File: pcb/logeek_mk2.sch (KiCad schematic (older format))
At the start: 136 parts, among them P1 Power, P10 XH2.54-2P RA, P11 BARREL_JACK, P12 USB_B, P13 DC3 5x2, P14 Power, P15 Analog, P16 Digital, P17 Digital, P2 Analog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

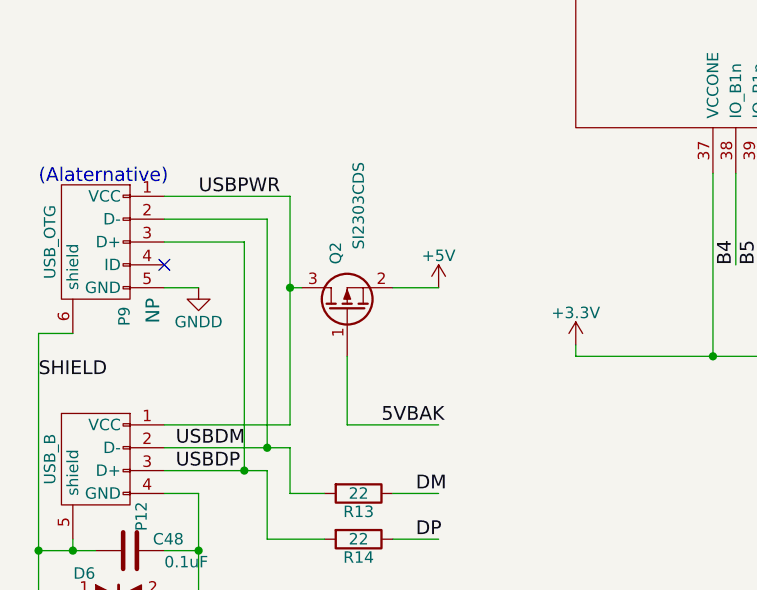
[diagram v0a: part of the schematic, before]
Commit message: Fine-tune copper and silkscreen. Add a fuse on USB power input.
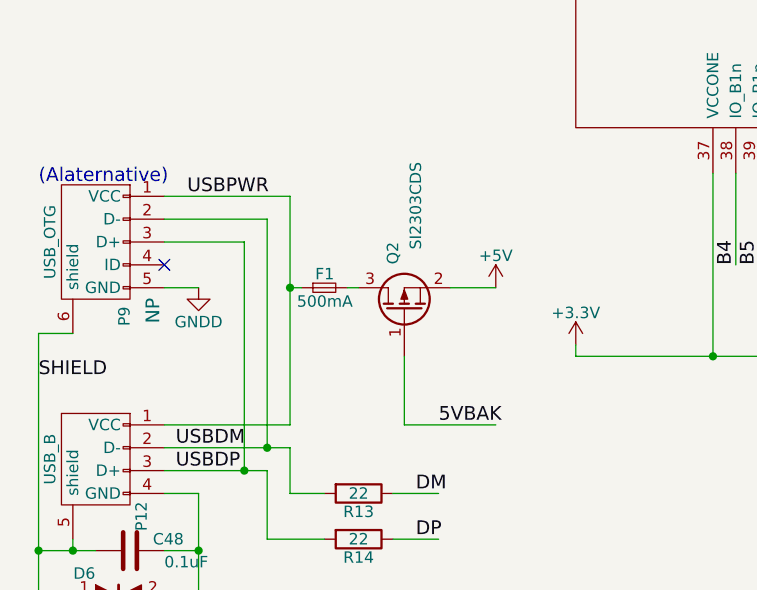
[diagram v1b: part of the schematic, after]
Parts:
- added F1: 500mA, Resistors_SMD:R_0603_HandSoldering, symbol F_Small
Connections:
- wire segments 545 -> 546
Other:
- moved on the sheet: Q2

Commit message: Power input socket changed to 5.08mm terminal.
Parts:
- P10: footprint Logeek_MK2:PINHEAD1-2 -> Logeek_MK2:DG301_2P_5.08mm_Straight
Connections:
- net labels removed: A8
- wire segments 546 -> 545
- no-connect marks 24 -> 25

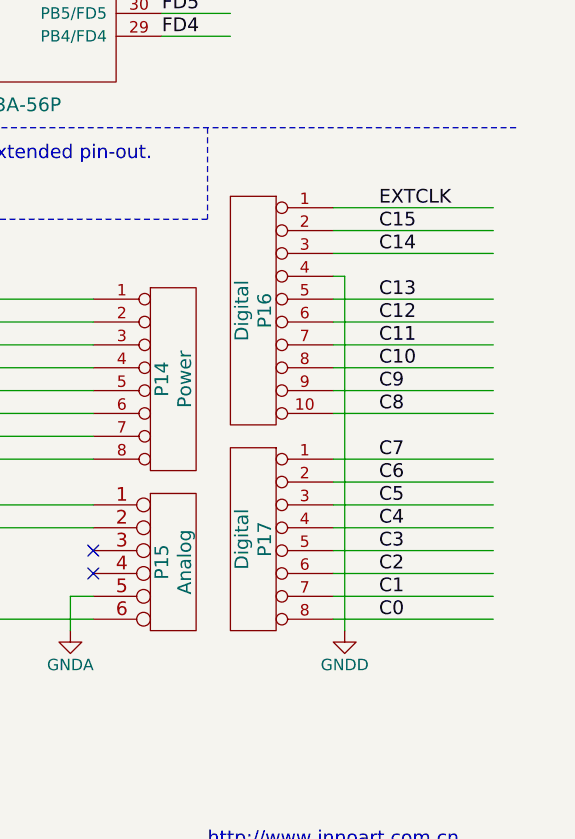
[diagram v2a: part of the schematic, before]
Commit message: C14,C15,CLK and GND pins changed.
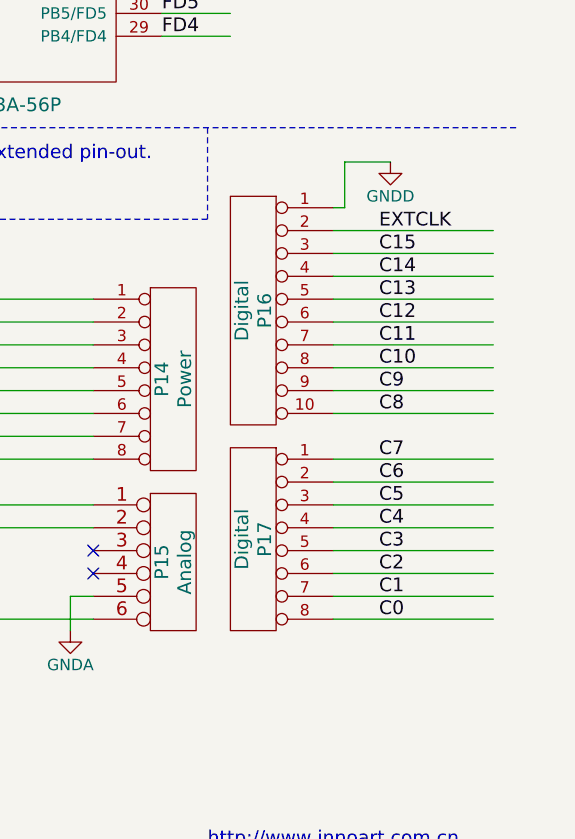
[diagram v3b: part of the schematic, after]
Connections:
- wire segments 545 -> 546
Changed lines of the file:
@@
 Text Label 15450 8150 0    60   ~ 0
 C13
-Text Label 15450 7950 0    60   ~ 0
+Text Label 15450 8050 0    60   ~ 0
 C14
-Text Label 15450 7850 0    60   ~ 0
+Text Label 15450 7950 0    60   ~ 0
 C15
 $Comp
 L GNDD #PWR0104
 U 1 1 55B9ECF4
-P 15300 9600
-F 0 "#PWR0104" H 15300 9350 50  0001 C CNN
-F 1 "GNDD" H 15300 9450 50  0000 C CNN
-F 2 "" H 15300 9600 60  0000 C CNN
-F 3 "" H 15300 9600 60  0000 C CNN
-	1    15300 9600
+P 15500 7550
+F 0 "#PWR0104" H 15500 7300 50  0001 C CNN
+F 1 "GNDD" H 15500 7400 50  0000 C CNN
+F 2 "" H 15500 7550 60  0000 C CNN
+F 3 "" H 15500 7550 60  0000 C CNN
+	1    15500 7550
 	1    0    0    -1
 $EndComp
-Text Label 15450 7750 0    60   ~ 0
+Text Label 15450 7850 0    60   ~ 0
 EXTCLK
 $Comp
@@
 Connection ~ 1100 8900
 Wire Wire Line
-	15300 8050 15300 9600
-Wire Wire Line
-	15950 7750 15250 7750
-Wire Wire Line
 	15950 7850 15250 7850
 Wire Wire Line
@@
 	13450 9550 14200 9550
 Wire Wire Line
-	15300 8050 15250 8050
-Wire Wire Line
 	14100 9450 14200 9450
 Wire Notes Line
@@
 	2350 7750 2300 7750
 NoConn ~ 14200 9250
+Wire Wire Line
+	15950 8050 15250 8050
+Wire Wire Line
+	15250 7750 15300 7750
+Wire Wire Line
+	15300 7750 15300 7550
+Wire Wire Line
+	15300 7550 15500 7550
 $EndSCHEMATC

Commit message: Power supplies redesigned.
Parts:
- removed D2, D7: 1N5819WS, Diodes_SMD:SOD-123, symbol D_Schottky
- removed D4, D8: 1N4148WS, Diodes_SMD:SOD-323, symbol D_Schottky
- removed F1: 500mA, Resistors_SMD:R_0603_HandSoldering, symbol F_Small
- removed R13, R14: 22, Resistors_SMD:R_0402_HandSoldering, symbol R
- removed R31: 1000k, Resistors_SMD:R_0402_HandSoldering, symbol R
- removed R39: 10k, Resistors_SMD:R_0402_HandSoldering, symbol R
- added L3: DLW21SN900SQ2, Logeek_MK2:CommonModeChoke_0805, symbol CMCC
- added Q1: SI2302CDS, Housings_SOT-23_SOT-143_TSOT-6:SOT-23, symbol Q_NMOS_GSD
- C18: footprint Capacitors_SMD:C_0805 -> Capacitors_SMD:C_1206
- C47: footprint Logeek_MK2:TantalC_SizeB_EIA-3528_HandSoldering -> Capacitors_Tantalum_SMD:TantalC_SizeT_EIA-3528
- D1, D3: value 1N5819WS -> B230A; footprint Diodes_SMD:SOD-123 -> Diodes_SMD:Diode-SMA_Standard
- D5: value LED TRUE GREEN -> LED GREEN
- P10: value XH2.54-2P RA -> DG301-2P 5.08mm
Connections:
- net labels removed: VIN_SAFE, WAKEUP
- wire segments 546 -> 540
- no-connect marks 25 -> 26
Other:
- moved on the sheet: C18, C19, C20, C21, C22, C24, C33, C39, C47, D1, D3, D5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

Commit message: Minor footprint change.
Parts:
- D6, R5: footprint Logeek_MK2:R_0402_HandSoldering -> Resistors_SMD:R_0402_HandSoldering
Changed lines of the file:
@@
 F 0 "D6" H 1150 9200 50  0000 C CNN
 F 1 "TVS 10 V" H 1350 9000 50  0000 C CNN
-F 2 "Logeek_MK2:R_0402_HandSoldering" H 1300 9100 60  0001 C CNN
+F 2 "Resistors_SMD:R_0402_HandSoldering" H 1300 9100 60  0001 C CNN
 F 3 "" H 1300 9100 60  0000 C CNN
 	1    1300 9100
@@
 00 39 19 59 AF 35 42 7E F6 69 BC 65 B4 12 E9 FA 23 84 AE 83 6F 0F D1 9A 40 57 B7 F2 6C 29 EA 3A
 9E 6A A1 85 FF 38 9C BE D1 9C BA 77 9F E3 4F 15 EE 64 AF AB 31 A7 47 CD F6 48 3D E9 C1 75 26 7B
-81 F3 EA B7 E7 8B FF 0F 20 F4 78 B9 DD 14 EB 4B 00 00 00 00 49 45 4E 44 AE 42 60 82 5D
+81 F3 EA B7 E7 8B FF 0F 20 F4 78 B9 DD 14 EB 4B 00 00 00 00 49 45 4E 44 AE 42 60 82 D2
 EndData
 $EndBitmap
@@
 F 0 "R5" V 10080 1650 50  0000 C CNN
 F 1 "1k" V 10000 1650 50  0000 C CNN
-F 2 "Logeek_MK2:R_0402_HandSoldering" V 9930 1650 30  0001 C CNN
+F 2 "Resistors_SMD:R_0402_HandSoldering" V 9930 1650 30  0001 C CNN
 F 3 "" H 10000 1650 30  0000 C CNN
 	1    10000 1650

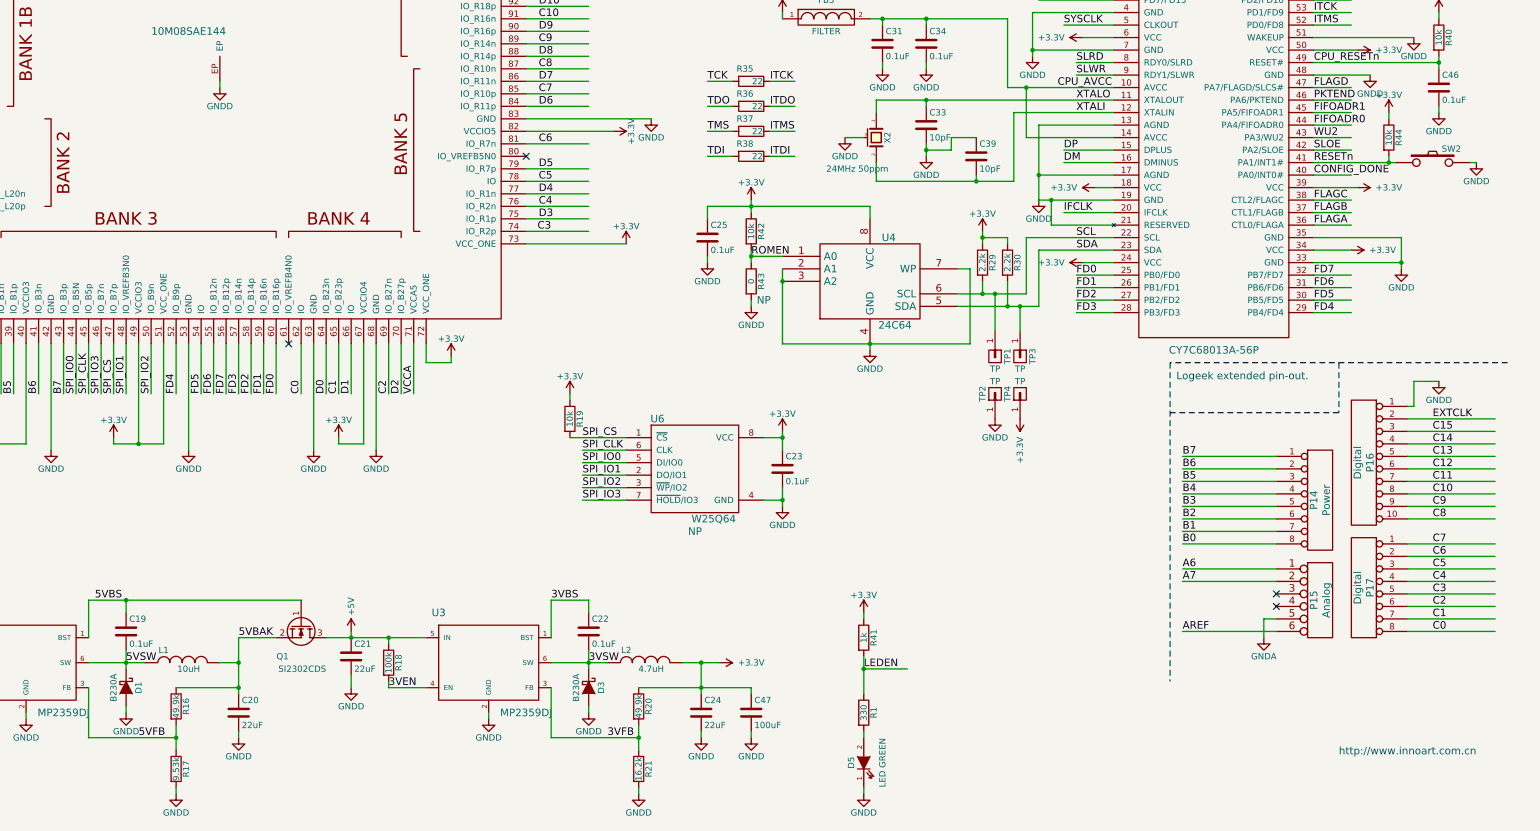
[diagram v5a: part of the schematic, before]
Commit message: Power switching circuit updated for safety issue.
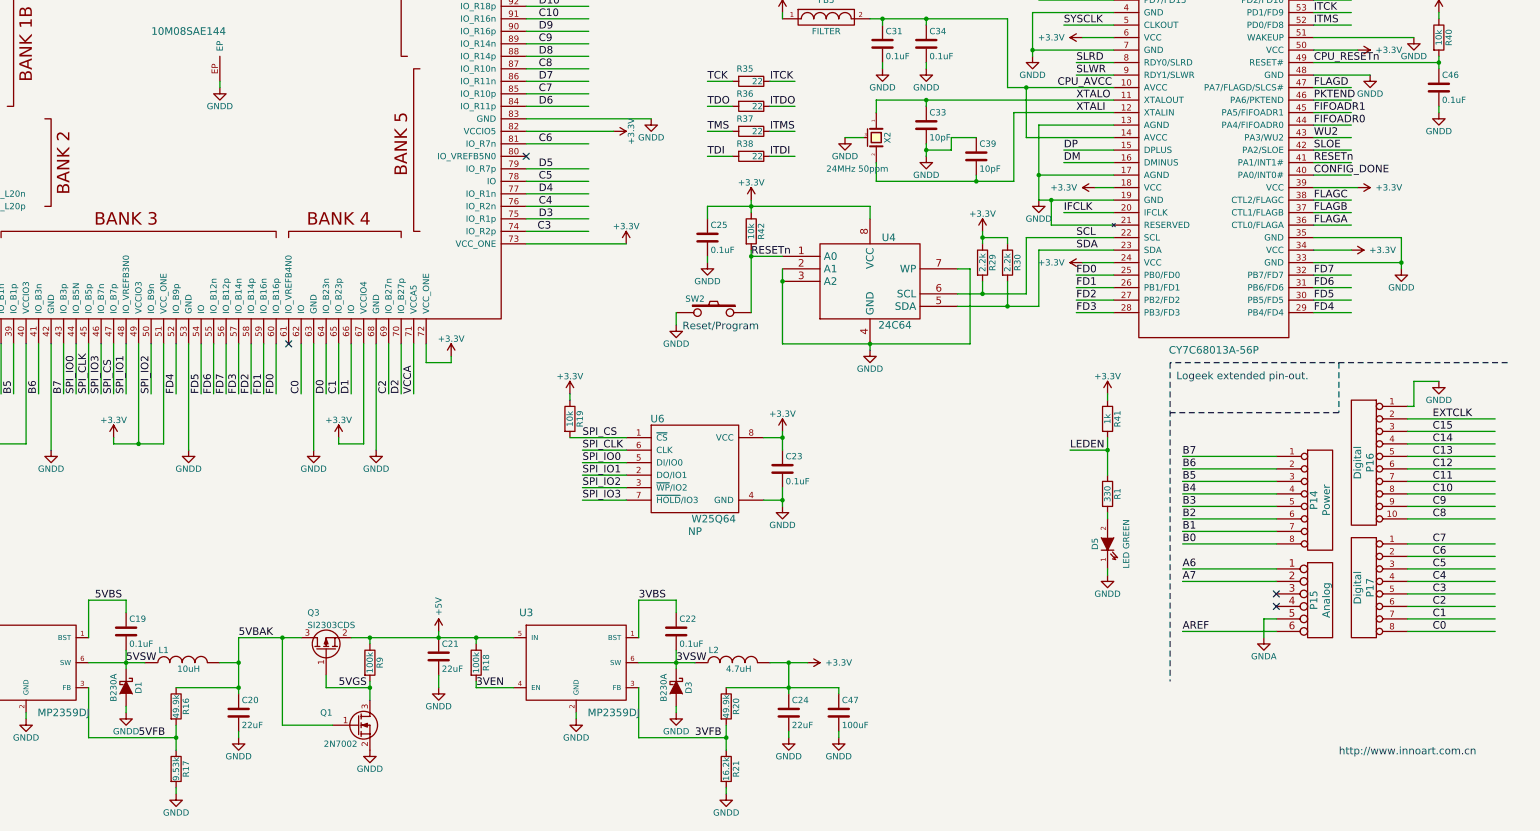
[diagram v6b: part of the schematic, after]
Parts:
- removed R43: 0, Resistors_SMD:R_0402_HandSoldering, symbol R
- removed R44: 10k, Resistors_SMD:R_0402_HandSoldering, symbol R
- removed TP1, TP2, TP3, TP4: TP, Logeek_MK2:Test_Point_1Pin, symbol CONN_01X01
- added Q3: SI2303CDS, Housings_SOT-23_SOT-143_TSOT-6:SOT-23, symbol Q_PMOS_GSD
- added R9: 100k, Resistors_SMD:R_0402_HandSoldering, symbol R
- Q1: value SI2302CDS -> 2N7002
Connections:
- net labels added: 5VGS
- net labels removed: ROMEN
- wire segments 540 -> 541
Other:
- note added: "Reset/Program"
- moved on the sheet: C21, C22, C24, C47, D3, D5, L2, Q1, R1, R18, R20, R21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

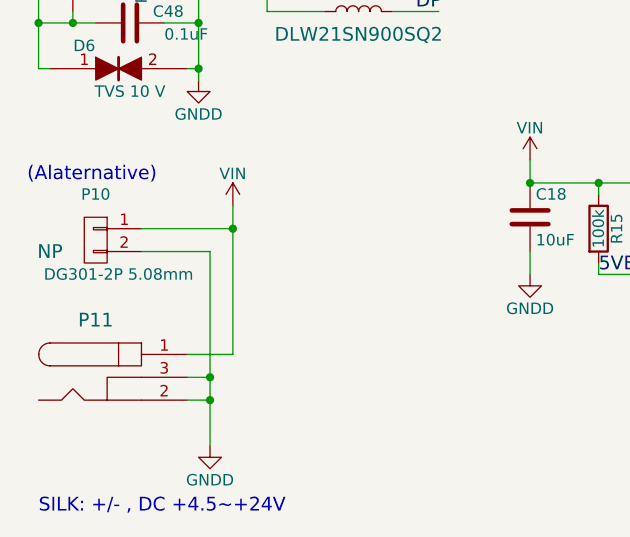
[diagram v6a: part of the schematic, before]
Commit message: Add a fuse to protest against VIN short-circuit.
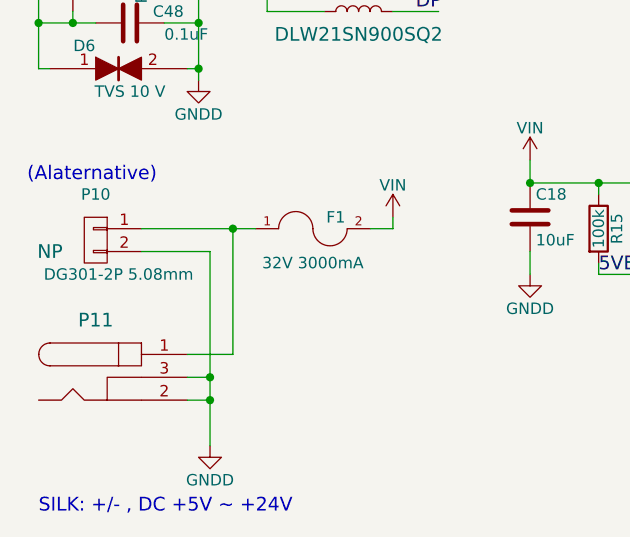
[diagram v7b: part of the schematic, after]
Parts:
- added F1: 32V 3000mA, Fuse_Holders_and_Fuses:Fuse_SMD1206_Wave, symbol FUSE
- C47: footprint Capacitors_Tantalum_SMD:TantalC_SizeT_EIA-3528 -> Capacitors_SMD:c_elec_5x5.8
- L1, L2: footprint Inductors:SELF-WE-TPC_M -> Logeek_MK2:Inductor_SM-2020
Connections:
- wire segments 541 -> 543
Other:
- note added: "SILK: +/- , DC +5V ~~ +24V"
- note removed: "SILK: +/- , DC +4.5~~+24V"
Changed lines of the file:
@@
 (Alaternative)
 Text Notes 950  11050 0    60   ~ 0
-SILK: +/- , DC +4.5~~+24V
+SILK: +/- , DC +5V ~~ +24V
 $Comp
 L CRYSTAL_SMD X2
@@
 F 0 "L1" V 5550 9950 50  0000 C CNN
 F 1 "10uH" V 5400 9750 50  0000 C CNN
-F 2 "Inductors:SELF-WE-TPC_M" H 5450 9800 60  0001 C CNN
+F 2 "Logeek_MK2:Inductor_SM-2020" H 5450 9800 60  0001 C CNN
 F 3 "" H 5450 9800 60  0000 C CNN
 	1    5450 9800
@@
 F 0 "L2" V 9950 9950 50  0000 C CNN
 F 1 "4.7uH" V 9800 9750 50  0000 C CNN
-F 2 "Inductors:SELF-WE-TPC_M" H 9850 9800 60  0001 C CNN
+F 2 "Logeek_MK2:Inductor_SM-2020" H 9850 9800 60  0001 C CNN
 F 3 "" H 9850 9800 60  0000 C CNN
 	1    9850 9800
@@
 F 0 "C47" H 10725 10300 50  0000 L CNN
 F 1 "100uF" H 10725 10100 50  0000 L CNN
-F 2 "Capacitors_Tantalum_SMD:TantalC_SizeT_EIA-3528" H 10738 10050 30  0001 C CNN
+F 2 "Capacitors_SMD:c_elec_5x5.8" H 10738 10050 30  0001 C CNN
 F 3 "" H 10700 10200 60  0000 C CNN
 	1    10700 10200
@@
 00 39 19 59 AF 35 42 7E F6 69 BC 65 B4 12 E9 FA 23 84 AE 83 6F 0F D1 9A 40 57 B7 F2 6C 29 EA 3A
 9E 6A A1 85 FF 38 9C BE D1 9C BA 77 9F E3 4F 15 EE 64 AF AB 31 A7 47 CD F6 48 3D E9 C1 75 26 7B
-81 F3 EA B7 E7 8B FF 0F 20 F4 78 B9 DD 14 EB 4B 00 00 00 00 49 45 4E 44 AE 42 60 82 39
+81 F3 EA B7 E7 8B FF 0F 20 F4 78 B9 DD 14 EB 4B 00 00 00 00 49 45 4E 44 AE 42 60 82 3E
 EndData
 $EndBitmap
@@
 L VIN #PWR0112
 U 1 1 56769E93
-P 1800 9700
-F 0 "#PWR0112" H 1800 9550 50  0001 C CNN
-F 1 "VIN" H 1800 9840 50  0000 C CNN
-F 2 "" H 1800 9700 60  0000 C CNN
-F 3 "" H 1800 9700 60  0000 C CNN
-	1    1800 9700
+P 2500 9750
+F 0 "#PWR0112" H 2500 9600 50  0001 C CNN
+F 1 "VIN" H 2500 9890 50  0000 C CNN
+F 2 "" H 2500 9750 60  0000 C CNN
+F 3 "" H 2500 9750 60  0000 C CNN
+	1    2500 9750
 	1    0    0    -1
 $EndComp
@@
 	2050 8350 1500 8350
 Wire Wire Line
-	1800 9700 1800 10350
-Wire Wire Line
 	14100 9600 14100 9450
 Wire Wire Line
@@
 	15300 7550 15500 7550
 Wire Wire Line
-	1800 9800 1400 9800
+	1400 9800 1900 9800
 Connection ~ 1800 9800
 Wire Wire Line
@@
 Text Label 6700 10000 0    60   ~ 0
 5VGS
+$Comp
+L FUSE F1
+U 1 1 567C2041
+P 2150 9800
+F 0 "F1" H 2250 9850 50  0000 C CNN
+F 1 "32V 3000mA" H 2150 9650 50  0000 C CNN
+F 2 "Fuse_Holders_and_Fuses:Fuse_SMD1206_Wave" H 2150 9800 60  0001 C CNN
+F 3 "" H 2150 9800 60  0000 C CNN
+	1    2150 9800
+	1    0    0    -1
+$EndComp
+Wire Wire Line
+	2400 9800 2500 9800
+Wire Wire Line
+	2500 9800 2500 9750
+Wire Wire Line
+	1800 10350 1800 9800
 $EndSCHEMATC

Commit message: Final revise before fabrication of Rev.B
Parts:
- L3: value DLW21SN900SQ2 -> DLW31SN222SQ2; footprint Logeek_MK2:CommonModeChoke_0805 -> Logeek_MK2:CommonModeChoke_1206
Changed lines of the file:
@@
 00 39 19 59 AF 35 42 7E F6 69 BC 65 B4 12 E9 FA 23 84 AE 83 6F 0F D1 9A 40 57 B7 F2 6C 29 EA 3A
 9E 6A A1 85 FF 38 9C BE D1 9C BA 77 9F E3 4F 15 EE 64 AF AB 31 A7 47 CD F6 48 3D E9 C1 75 26 7B
-81 F3 EA B7 E7 8B FF 0F 20 F4 78 B9 DD 14 EB 4B 00 00 00 00 49 45 4E 44 AE 42 60 82 3E
+81 F3 EA B7 E7 8B FF 0F 20 F4 78 B9 DD 14 EB 4B 00 00 00 00 49 45 4E 44 AE 42 60 82 8E
 EndData
 $EndBitmap
@@
 P 2350 8750
 F 0 "L3" H 2250 8950 60  0000 C CNN
-F 1 "DLW21SN900SQ2" H 2350 8550 60  0000 C CNN
-F 2 "Logeek_MK2:CommonModeChoke_0805" H 2350 8750 60  0001 C CNN
+F 1 "DLW31SN222SQ2" H 2350 8550 60  0000 C CNN
+F 2 "Logeek_MK2:CommonModeChoke_1206" H 2350 8750 60  0001 C CNN
 F 3 "" H 2350 8750 60  0000 C CNN
 	1    2350 8750
